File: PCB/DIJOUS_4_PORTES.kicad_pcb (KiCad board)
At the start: 2 copper layers, 96.9 x 106.2 mm, 68 parts, among them J1 PowerIN, J10 DOOR_LCK, J12 WIN_SW, J14 FINAL_CARRERA_UP, J15 FINAL_CARRERA_DOWN, J2 OUT_WIN, J3 ICSP, J4 CAN, J5 OUT_DOOR, J6 USART, J7 SPI, J8 RFID_COAX, SW1 DOOR_LCK, SW3 WIN_SW, U1 LT1528CT-PBF, U2 PIC32MK0256MCJ048-I/Y8X, U3 TCAN334D, U4 MAX22201ATC+, U5 MAX22201ATC+, Y1 ASZKDV-32.768KHZ-L-T3, Y2 ECS-3225SMV-080-GP-TR

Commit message: canvis i arreglos
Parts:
- moved Y1 0.16 mm to (198.4, 99.9)
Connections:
- U2 pad 38: DOOR_IN2 -> FINAL_CARRERA_UP
- U2 pad 39: FINAL_CARRERA_UP -> DOOR_IN1
- U2 pad 40: DOOR_IN1 -> DOOR_IN2
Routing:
- net GND: track 26.0 -> 45.8 mm, vias 75 -> 81
- net FINAL_CARRERA_DOWN: track 55.1 -> 58.2 mm, vias 0 -> 1
- net FINAL_CARRERA_UP: track 51.7 -> 49.3 mm, vias 0 -> 1
- net DOOR_IN1: track 35.8 -> 34.8 mm
- net DOOR_IN2: track 34.7 -> 35.5 mm
- net /FAULT_DOOR: track 42.0 -> 42.6 mm

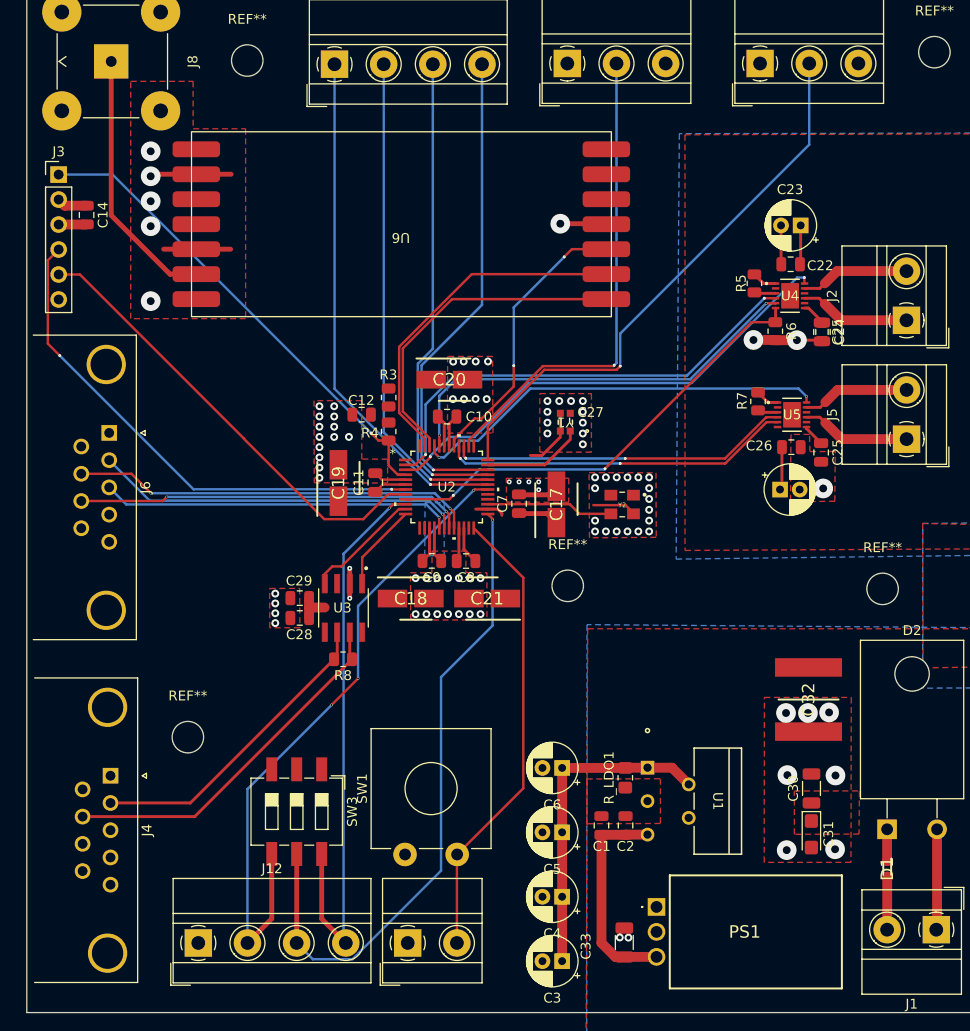
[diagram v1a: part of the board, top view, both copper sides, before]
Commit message: Solució d'errors DRC
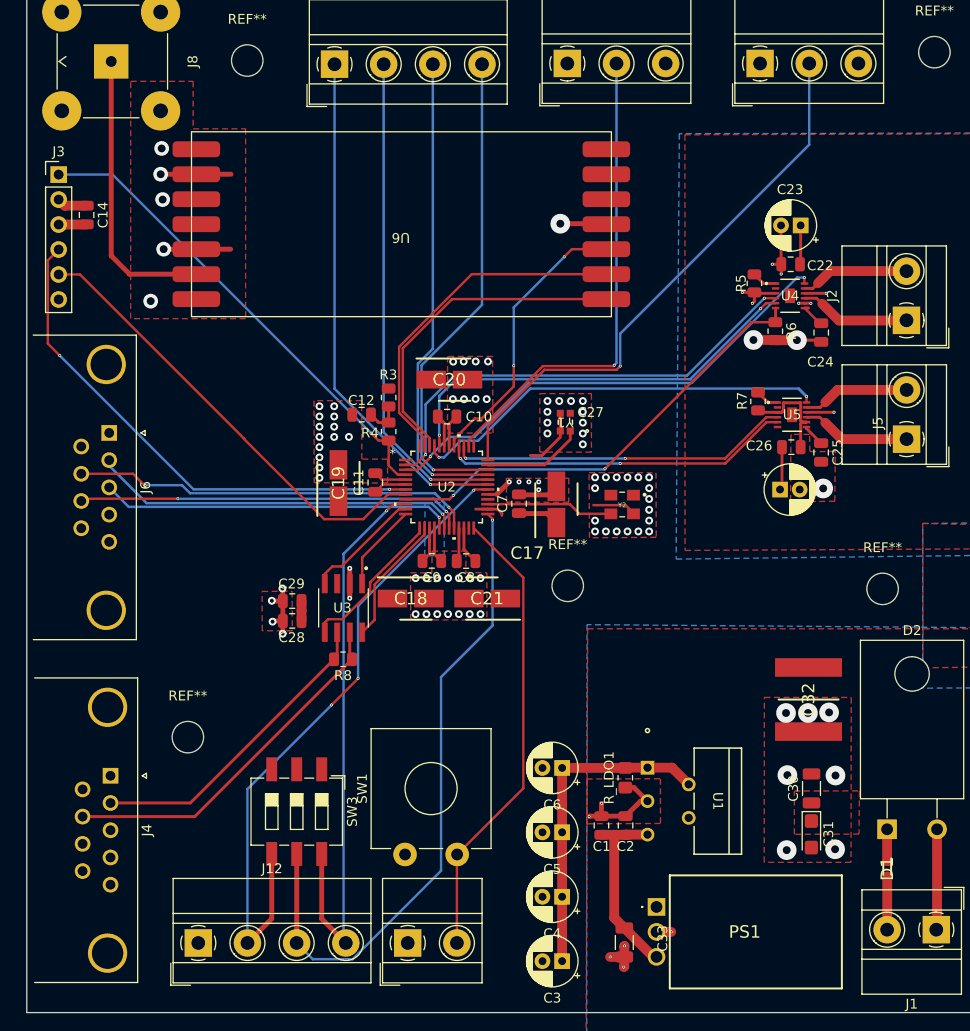
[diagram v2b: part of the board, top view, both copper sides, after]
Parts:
- removed the C25 at (224.4, 90.8)
- moved C28 0.83 mm to (170.6, 120.2)
- moved C29 0.83 mm to (170.6, 118.1)
- moved C24 0.19 mm to (224.4, 90.8)
- turned C33 to -90 degrees
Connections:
- C1 pad 2: GND -> GNDPWR
- C2 pad 2: GND -> GNDPWR
- C33 pad 2: GND -> GNDPWR
- R_LDO1 pad 1: GND -> GNDPWR
- U1 pad 3: GND -> GNDPWR
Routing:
- net GNDPWR: track 20.8 -> 50.9 mm, vias 12 -> 22
- net CAN_SHDN: track 0.00 -> 15.5 mm
- net CAN_STB: track 0.00 -> 13.2 mm
- net GND: track 45.8 -> 52.0 mm
- net +12V: track 11.8 -> 16.8 mm, vias 0 -> 2
- net /DIGITAL/MCLR_VDD: track 0.00 -> 3.78 mm
- net /DIGITAL/RF_out: track 26.8 -> 29.2 mm
- net +5V: track 21.9 -> 19.6 mm
- net +3.3V: track 72.1 -> 70.6 mm

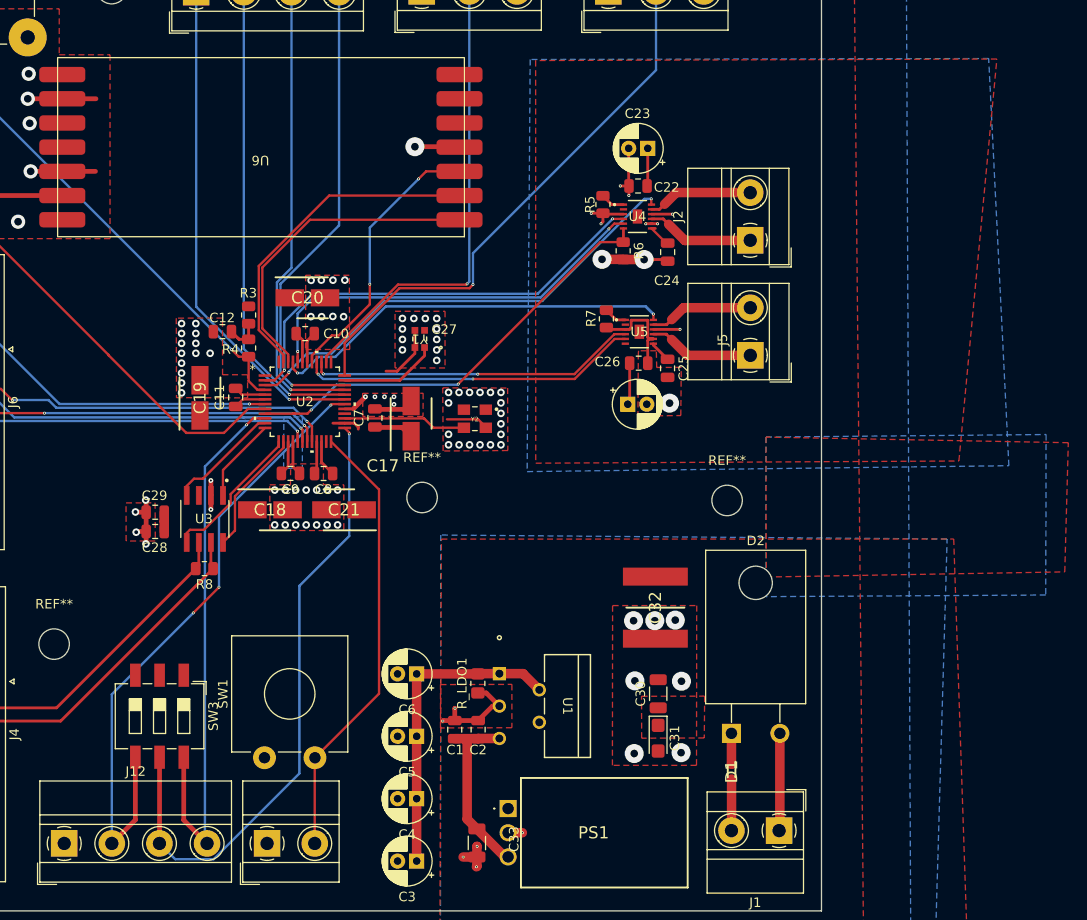
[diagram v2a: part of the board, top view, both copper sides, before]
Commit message: Add files via upload
Arreglat DRC i afegit noms
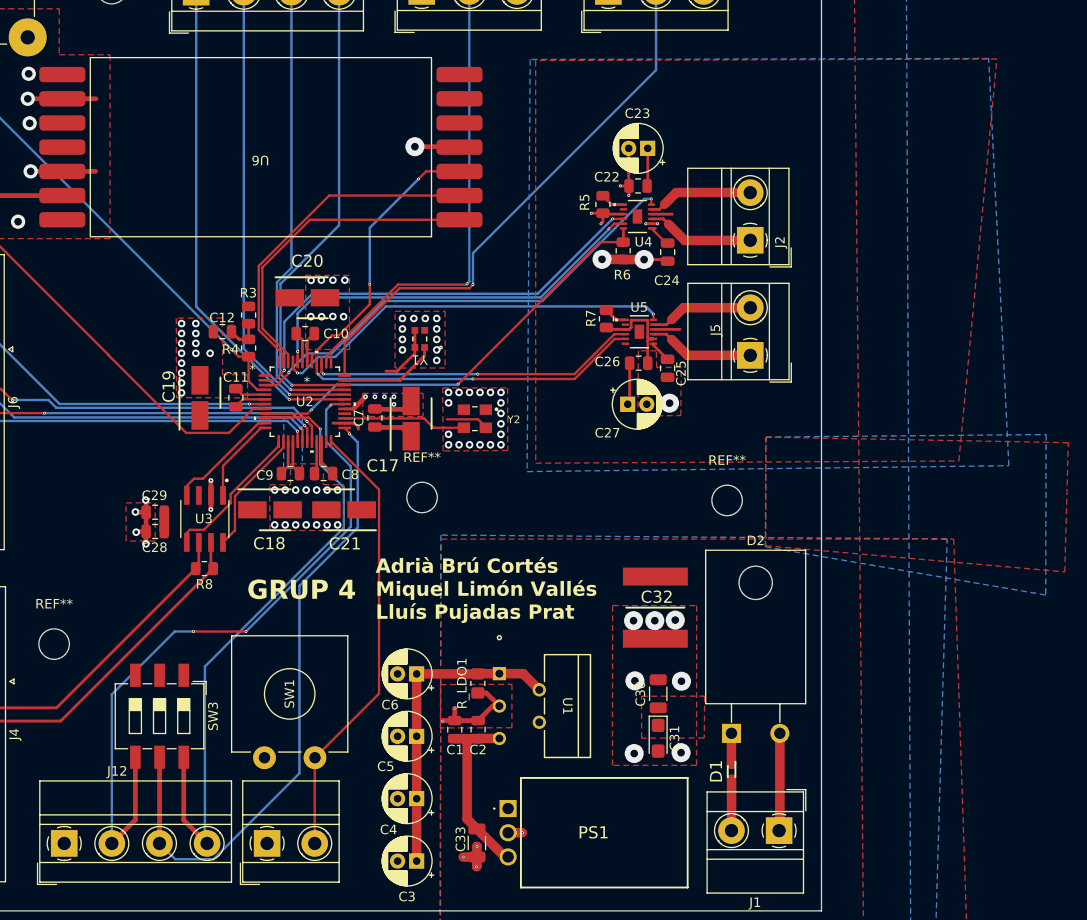
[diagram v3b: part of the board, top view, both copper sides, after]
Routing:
- net WIN_SW3: track 57.7 -> 67.6 mm
- net WIN_SW1: track 67.1 -> 73.6 mm
- net WIN_SW2: track 66.8 -> 67.5 mm
- net +12V: track 16.8 -> 16.7 mm, vias 2 -> 0
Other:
- board text added: "Adrià Brú Cortés Miquel Limón Vallés Lluís Pujadas Prat"
- board text added: "GRUP 4"

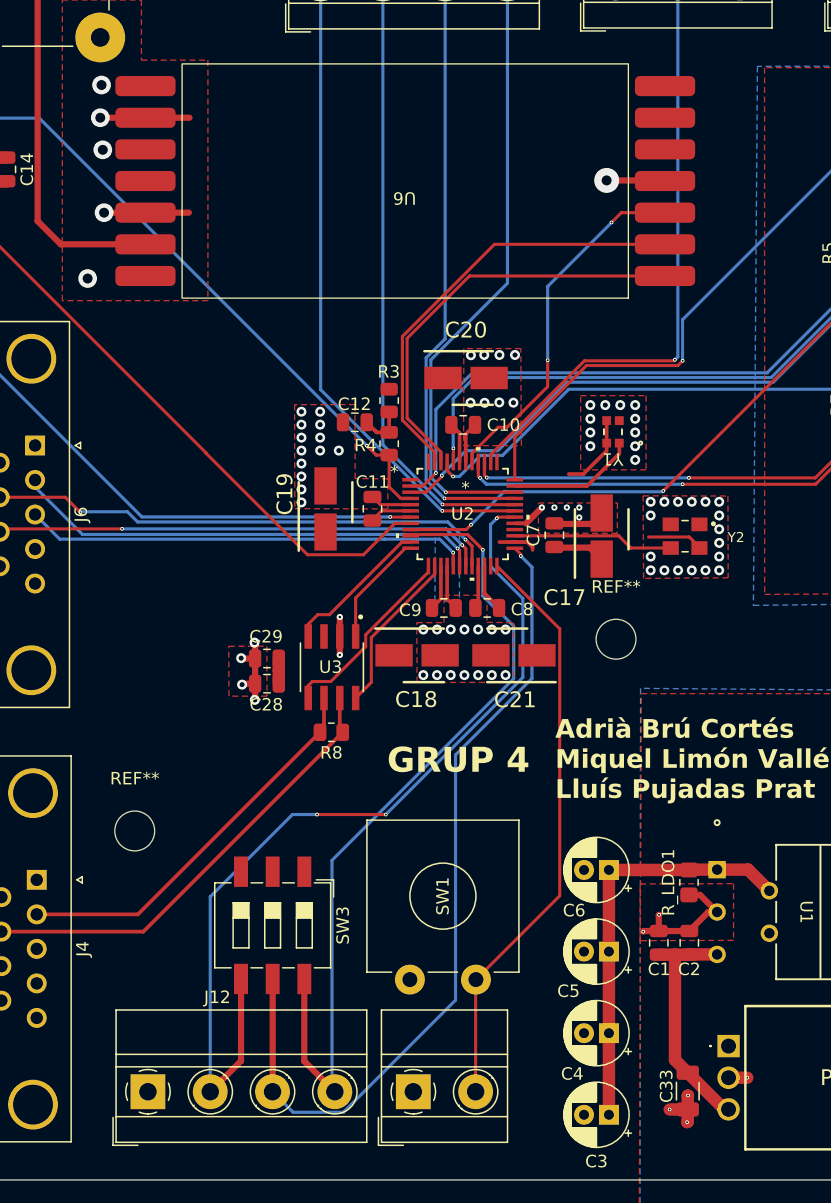
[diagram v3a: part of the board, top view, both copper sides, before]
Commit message: matrius de gnd
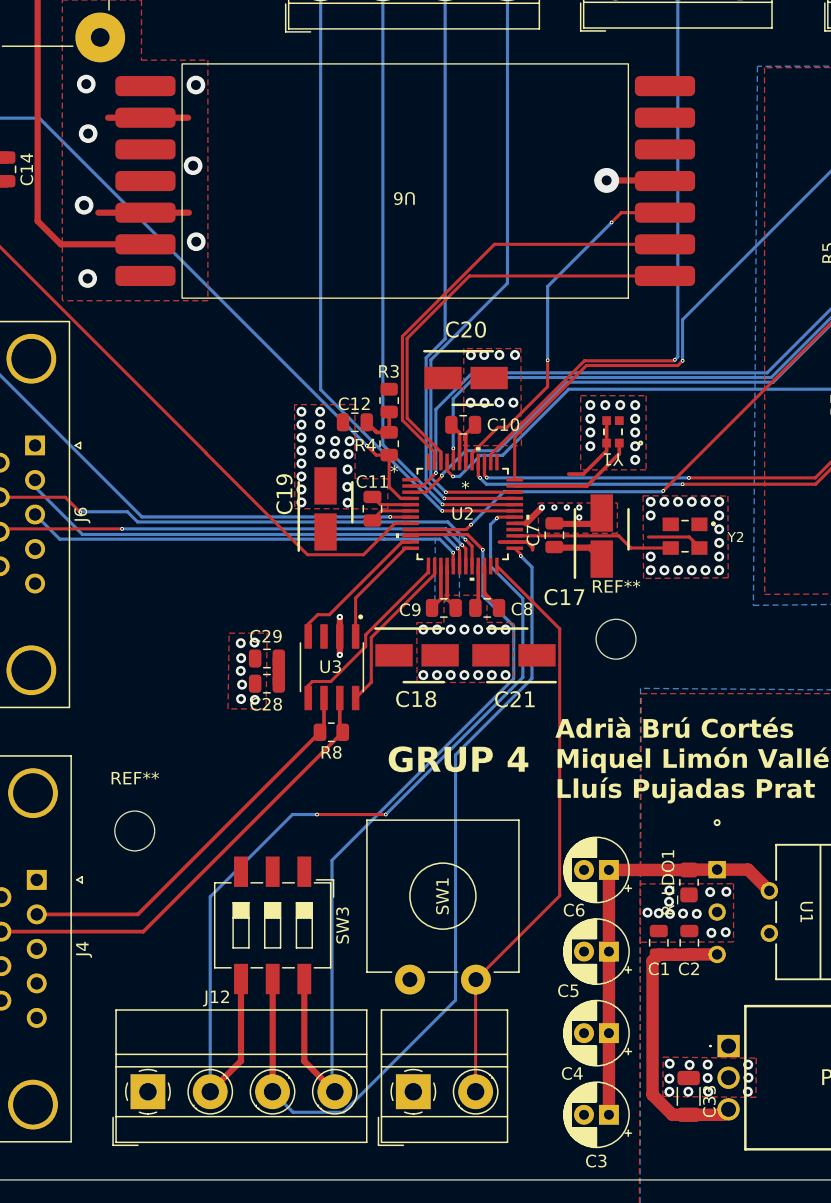
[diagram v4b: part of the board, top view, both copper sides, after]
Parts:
- moved C33 0.43 mm to (204.4, 153.3), turned to 90 degrees
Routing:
- net GNDPWR: track 50.9 -> 35.4 mm, vias 22 -> 38
- net GND: track 52.0 -> 45.1 mm, vias 81 -> 92
- net +5V: track 19.6 -> 23.6 mm
